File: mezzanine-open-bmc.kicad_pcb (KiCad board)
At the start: 2 copper layers, 85 x 54.1 mm, 53 parts, among them P1 CONN_02X20, P2 CONN_02X20, P3 CONN_01X04, P4 CONN_01X04, SW1 PWR, SW2 RST, U1 FT230XS, U2 SOT223, U3 DS3231N, U4 PCA9306, U5 M24C16-WMN6P, U6 REG_1.8V, U7 TXS0104PW

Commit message: Complete Schematic & Start PCB Layout
Pulling all the changes in.

Signed-off-by: Sophie Haynes <sophie.haynes@linaro.org>
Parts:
- added C16: 0.1n, Capacitors_SMD:C_0603, F.Cu at (151.4, 117.2)
- added C17: 0.1n, Capacitors_SMD:C_0603, F.Cu at (159.1, 114.8)
- added P5: CONN_01X04, 96boards:Grove_SMD_Connector, F.Cu at (205.2, 138.2)
- added R12: 2.2K, Resistors_SMD:R_0603, F.Cu at (156.2, 117.2)
- added R14: 2.2K, Resistors_SMD:R_0603, F.Cu at (149.8, 117.2)
- added R15: 2.2K, Resistors_SMD:R_0603, F.Cu at (158.0, 117.2)
- added R16: 200k, Resistors_SMD:R_0603, F.Cu at (150.5, 119.5)
- added R21: 200k, Resistors_SMD:R_0603, F.Cu at (159.6, 117.3)
- added R22: 0R, Resistors_SMD:R_1206, F.Cu at (162.0, 166.0)
- added R9: 2.2K, Resistors_SMD:R_0603, F.Cu at (148.1, 117.2)
- added U8: PCA9306, 96boards:PCA9306, F.Cu at (155.6, 111.9)
- C14, C15: value 100n -> 0.1n
- P3, P4: footprint 96boards:Grove4P -> 96boards:Grove_SMD_Connector
- R1, R13: value 90Ω -> 990R
- R10, R17: value 620R -> 22R
- U2: value SOT223 -> PMIC-CJT1117-3.3(SOT223)
- U7: value TXS0104PW -> PCA9306; footprint Housings_SSOP:SSOP-14_5.3x6.2mm_Pitch0.65mm -> 96boards:PCA9306
- moved U5 39.7 mm to (190.7, 122.0)
- moved C7 36.9 mm to (188.5, 115.8)
- moved C10 28.3 mm to (188.6, 107.3)
- moved C14 25.3 mm to (151.3, 109.7), turned to 90 degrees
- moved C15 25.1 mm to (155.6, 109.9), turned to 90 degrees
- moved U7 25.0 mm to (150.2, 112.0), turned to 0 degrees
- moved P4 24.0 mm to (206.8, 102.8), turned to 90 degrees
- moved P3 20.9 mm to (205.5, 120.8), turned to 90 degrees
- moved C9 15.7 mm to (153.2, 109.7)
- moved R6 15.4 mm to (107.5, 125.5)
- moved U4 14.2 mm to (152.9, 111.9), turned to 0 degrees
- moved C6 10.7 mm to (165.3, 123.2)
- moved U2 10.3 mm to (141.3, 118.5), turned to 90 degrees
- moved R18 9.86 mm to (152.9, 117.1), turned to 90 degrees
- moved C12 9.63 mm to (133.6, 126.5)
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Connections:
- C11 pad 1: Net-(C11-Pad1) -> +3V3_F
- C15 pad 1: +5V -> +1V8
- C6 pad 1: GND -> +5V
- C6 pad 2: +5V -> GND
- P3 pad 1: I2C0_SCL/5 -> I2C0_SCL_3.3
- P3 pad 2: I2C0_SDA/5 -> I2C0_SDA_3.3
- P3 pad 3: +5V -> +3V3
- P4 pad 1: I2C1_SCL/5 -> I2C1_SCL_3.3
- P4 pad 2: I2C1_SDA/5 -> I2C1_SDA_3.3
- P4 pad 3: +5V -> +3V3
- U1 pad 10: Net-(C11-Pad1) -> +3V3_F
- U1 pad 11: Net-(C11-Pad1) -> +3V3_F
- U5 pad 5: I2C0_SDA -> I2C0_SDA_3.3
- U5 pad 6: I2C0_SCL -> I2C0_SCL_3.3
- U7 pad 1: +1V8 -> GND
- U7 pad 2: I2C0_SDA -> +1V8
- U7 pad 3: I2C0_SCL -> I2C1_SCL_BMC
- U7 pad 4: I2C1_SDA -> I2C1_SDA_BMC
- U7 pad 5: I2C1_SCL -> I2C1_SDA_BMC_3.3
- U7 pad 6: Net-(U7-Pad6) -> I2C1_SCL_BMC_3.3
- U7 pad 7: GND -> Net-(C16-Pad1)
- U7 pad 8: +1V8 -> Net-(C16-Pad1)
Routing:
- net +1V8: track 187.7 -> 50.0 mm
- net +5V: track 166.3 -> 58.9 mm, vias 3 -> 2
- net GND: track 153.9 -> 75.6 mm
- net I2C0_SCL: track 72.4 -> 11.6 mm, vias 3 -> 2
- net I2C0_SDA: track 68.8 -> 10.6 mm
- net I2C1_SCL_BMC: track 0.00 -> 29.9 mm, vias 0 -> 1
- net PWR_BTN_BMC: track 19.0 -> 47.8 mm, vias 1 -> 2
- net I2C1_SDA_BMC: track 0.00 -> 27.9 mm, vias 0 -> 1
- net UART1_RX_BMC: track 26.2 -> 1.49 mm, vias 1 -> 0
- net Net-(BT1-Pad1): track 22.5 -> 0.00 mm, vias 1 -> 0
- net UART1_TX_BMC: track 20.6 -> 0.00 mm, vias 1 -> 0
- net I2C1_SCL: track 28.4 -> 10.5 mm, vias 2 -> 0
- net I2C1_SDA: track 27.3 -> 10.5 mm, vias 2 -> 0
- net I2C1_SCL/5: track 16.5 -> 0.00 mm
- net VBUS: track 15.9 -> 1.75 mm
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- added copper zone on B.Cu, net GND
- added copper zone on F.Cu, net GND
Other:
- board size 85 x 54.1 mm -> 85 x 54 mm

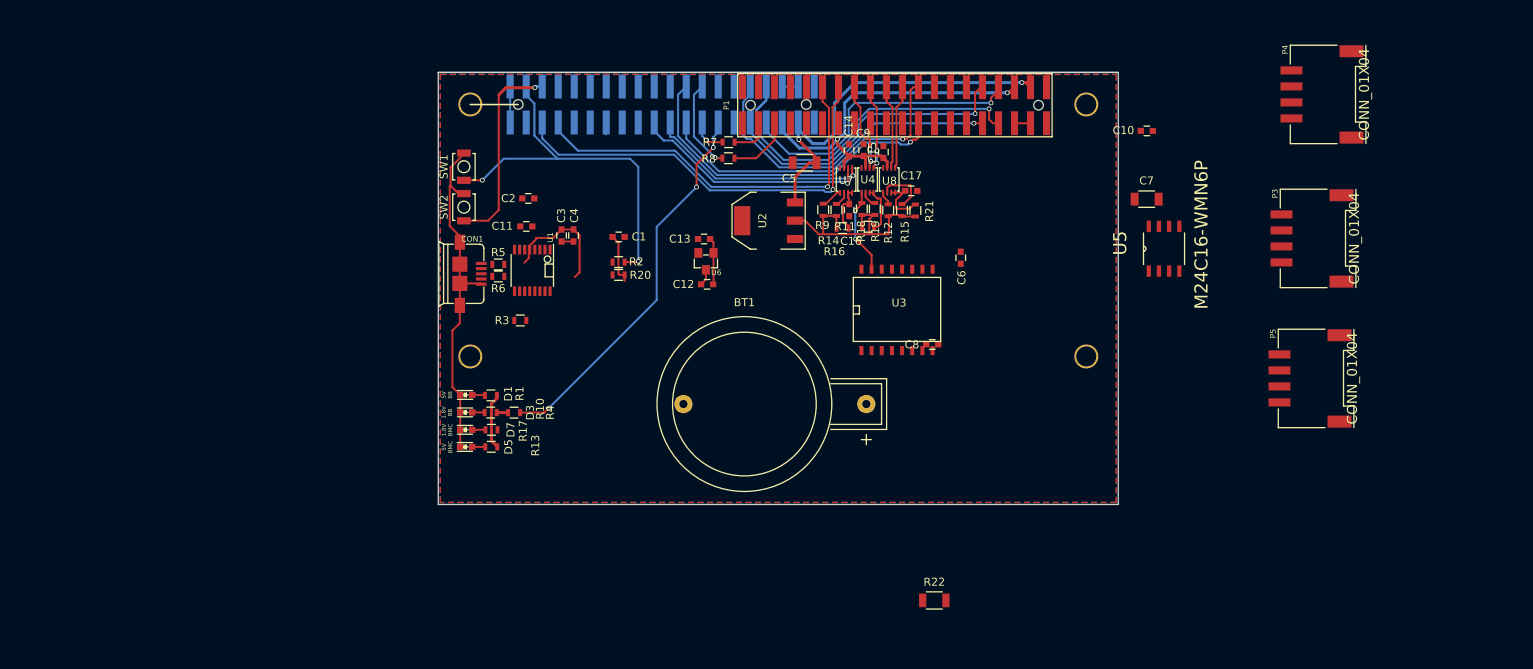
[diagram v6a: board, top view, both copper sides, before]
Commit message: Swap Location of P1/P2
The BMC board should be on the top, so the pin header have been switched
accordingly.

Signed-off-by: Sophie Haynes <sophie.haynes@linaro.org>
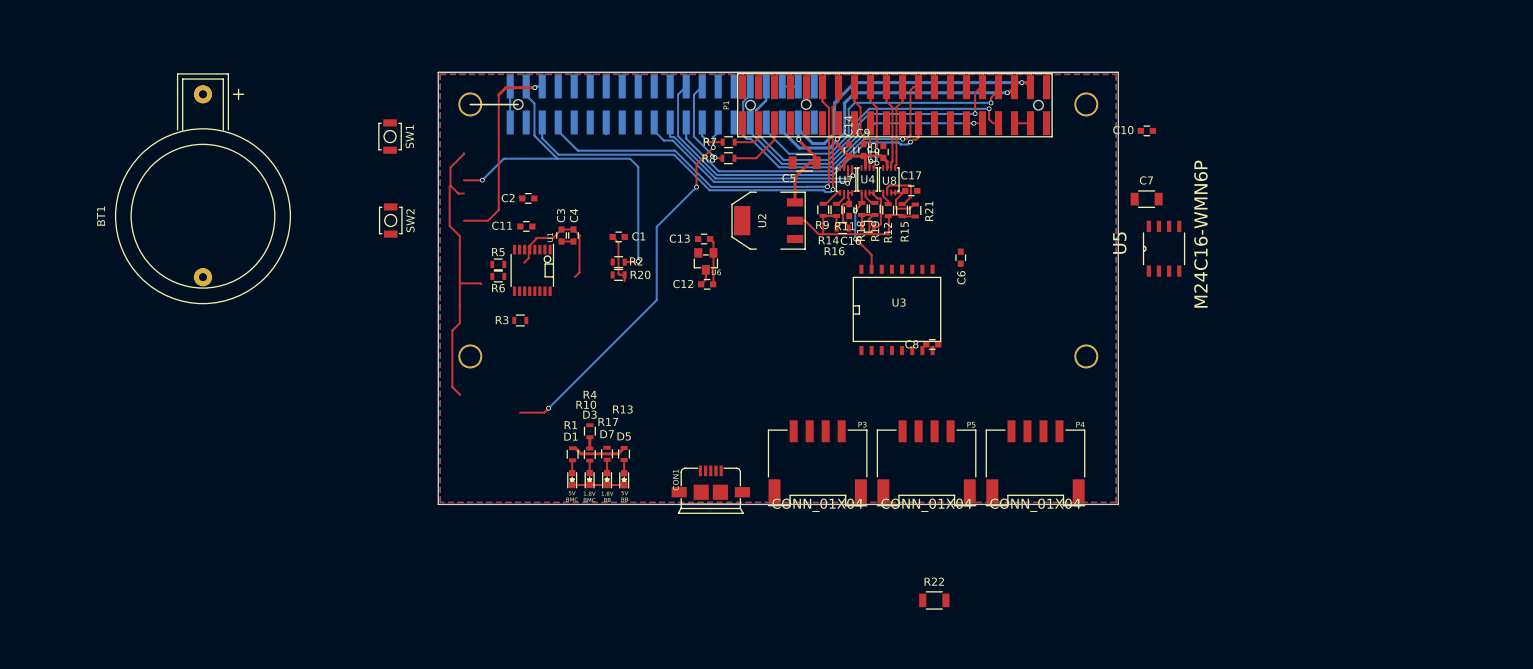
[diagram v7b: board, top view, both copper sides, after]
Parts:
- R11, R16, R21: value 200k -> 200K
- moved BT1 71.6 mm to (70.6, 118.0), turned to 90 degrees
- moved P3 62.9 mm to (147.4, 145.0), turned to 0 degrees
- moved P4 53.0 mm to (174.7, 145.0), turned to 0 degrees
- moved P5 44.7 mm to (161.0, 145.0), turned to 0 degrees
- moved CON1 43.7 mm to (134.1, 154.0), turned to 0 degrees
- moved D5 20.2 mm to (123.2, 150.8), turned to 90 degrees
- moved D7 18.7 mm to (121.1, 150.8), turned to 90 degrees
- moved D3 17.5 mm to (118.9, 150.8), turned to 90 degrees
- moved D1 16.9 mm to (116.7, 150.8), turned to 90 degrees
- moved R13 16.6 mm to (123.2, 147.7), turned to 270 degrees
- moved R17 14.8 mm to (121.1, 147.7), turned to 270 degrees
- moved R10 13.5 mm to (118.9, 147.8), turned to 270 degrees
- moved R1 12.6 mm to (116.8, 147.7), turned to 270 degrees
- moved SW1 9.97 mm to (94.0, 108.0), turned to 270 degrees
- moved R4 9.76 mm to (118.9, 144.8), turned to 90 degrees
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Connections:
- C1 pad 1: Net-(C1-Pad1) -> /USB+
- C2 pad 1: Net-(C2-Pad1) -> /USB-
- CON1 pad 2: Net-(C2-Pad1) -> /USB-
- CON1 pad 3: Net-(C1-Pad1) -> /USB+
- P1 pad 10: SPIO_DIN -> SPIO_DIN_BMC
- P1 pad 11: UART1_TX -> UART1_TX_BMC
- P1 pad 12: SPIO_CS -> SPIO_CS_BMC
- P1 pad 13: UART1_RX -> UART1_RX_BMC
- P1 pad 14: SPIO_DOUT -> SPIO_DOUT_BMC
- P1 pad 16: PCM_FS -> PCM_FS_BMC
- P1 pad 18: PCM_CLK -> PCM_CLK_BMC
- P1 pad 19: I2C1_SCL -> I2C1_SCL_BMC
- P1 pad 20: PCM_DO -> PCM_DO_BMC
- P1 pad 21: I2C1_SDA -> I2C1_SDA_BMC
- P1 pad 22: PCM_DI -> PCM_DI_BMC
- P1 pad 25: GPIO_C -> GPIO_C_BMC
- P1 pad 26: GPIO_D -> GPIO_D_BMC
- P1 pad 27: GPIO_E -> GPIO_E_BMC
- P1 pad 28: GPIO_F -> GPIO_F_BMC
- P1 pad 29: GPIO_G -> GPIO_G_BMC
- P1 pad 3: UART0_CTS -> Net-(P1-Pad3)
- P1 pad 30: GPIO_H -> GPIO_H_BMC
- P1 pad 36: SYS_DCIN -> SYS_DCIN_BMC
- P1 pad 38: SYS_DCIN -> SYS_DCIN_BMC
- P1 pad 4: PWR_BTN_N -> PWR_BTN_BMC
- P1 pad 5: UART0_TX -> UART1_RX
- P1 pad 6: RST_BTN_N -> RST_BTN_BMC
- P1 pad 7: UART0_RX -> UART1_TX
- P1 pad 8: SPIO_SCL -> SPIO_SCL_BMC
- P1 pad 9: UART0_RTS -> Net-(P1-Pad9)
- P2 pad 10: SPIO_DIN_BMC -> SPIO_DIN
- P2 pad 11: UART1_TX_BMC -> UART1_TX
- P2 pad 12: SPIO_CS_BMC -> SPIO_CS
- P2 pad 13: UART1_RX_BMC -> UART1_RX
- P2 pad 14: SPIO_DOUT_BMC -> SPIO_DOUT
- P2 pad 16: PCM_FS_BMC -> PCM_FS
- P2 pad 18: PCM_CLK_BMC -> PCM_CLK
- P2 pad 19: I2C1_SCL_BMC -> I2C1_SCL
- P2 pad 20: PCM_DO_BMC -> PCM_DO
- P2 pad 21: I2C1_SDA_BMC -> I2C1_SDA
- P2 pad 22: PCM_DI_BMC -> PCM_DI
- P2 pad 25: GPIO_C_BMC -> GPIO_C
- P2 pad 26: GPIO_D_BMC -> GPIO_D
- P2 pad 27: GPIO_E_BMC -> GPIO_E
- P2 pad 28: GPIO_F_BMC -> GPIO_F
- P2 pad 29: GPIO_G_BMC -> GPIO_G
- P2 pad 3: Net-(P2-Pad3) -> UART0_CTS
- P2 pad 30: GPIO_H_BMC -> GPIO_H
- P2 pad 36: SYS_DCIN_BMC -> SYS_DCIN
- P2 pad 38: SYS_DCIN_BMC -> SYS_DCIN
- P2 pad 4: PWR_BTN_BMC -> PWR_BTN_N
- P2 pad 5: UART1_RX -> UART0_TX
- P2 pad 6: RST_BTN_BMC -> RST_BTN_N
- P2 pad 7: UART1_TX -> UART0_RX
- P2 pad 8: SPIO_SCL_BMC -> SPIO_SCL
- P2 pad 9: Net-(P2-Pad9) -> UART0_RTS
- R14 pad 1: I2C1_SCL_BMC_3.3 -> +3V3
- R14 pad 2: +3V3 -> I2C1_SCL_BMC_3.3
- R15 pad 1: I2C1_SCL_3.3 -> +3V3
- R15 pad 2: +3V3 -> I2C1_SCL_3.3
- R19 pad 1: I2C0_SCL_3.3 -> +3V3
- R19 pad 2: +3V3 -> I2C0_SCL_3.3
- R5 pad 1: Net-(R5-Pad1) -> /USB-
- R5 pad 2: Net-(C2-Pad1) -> /USB-
- R6 pad 1: Net-(R6-Pad1) -> /USB+
- R6 pad 2: Net-(C1-Pad1) -> /USB+
- U1 pad 8: Net-(R6-Pad1) -> /USB+
- U1 pad 9: Net-(R5-Pad1) -> /USB-
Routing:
- net UART1_RX: track 55.4 -> 1.49 mm, vias 1 -> 0
- net UART1_TX: track 51.5 -> 0.00 mm, vias 1 -> 0
- net GPIO_E_BMC: track 48.3 -> 0.00 mm, vias 3 -> 0
- net GPIO_E: track 0.00 -> 48.3 mm, vias 0 -> 3
- net UART0_TX: track 0.00 -> 42.3 mm, vias 0 -> 1
- net UART0_RX: track 0.00 -> 37.6 mm, vias 0 -> 1
- net GND: track 75.6 -> 38.7 mm
- net (no net): track 0.00 -> 36.9 mm
- net I2C1_SDA_BMC: track 27.9 -> 3.23 mm
- net I2C1_SDA: track 10.5 -> 35.1 mm
- net RST_BTN_N: track 8.05 -> 31.1 mm, vias 0 -> 1
- net RST_BTN_BMC: track 25.2 -> 2.09 mm, vias 1 -> 0
- net UART1_TX_BMC: track 0.00 -> 13.9 mm
- net UART1_RX_BMC: track 1.49 -> 13.1 mm
- net GPIO_D_BMC: track 11.4 -> 0.97 mm
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
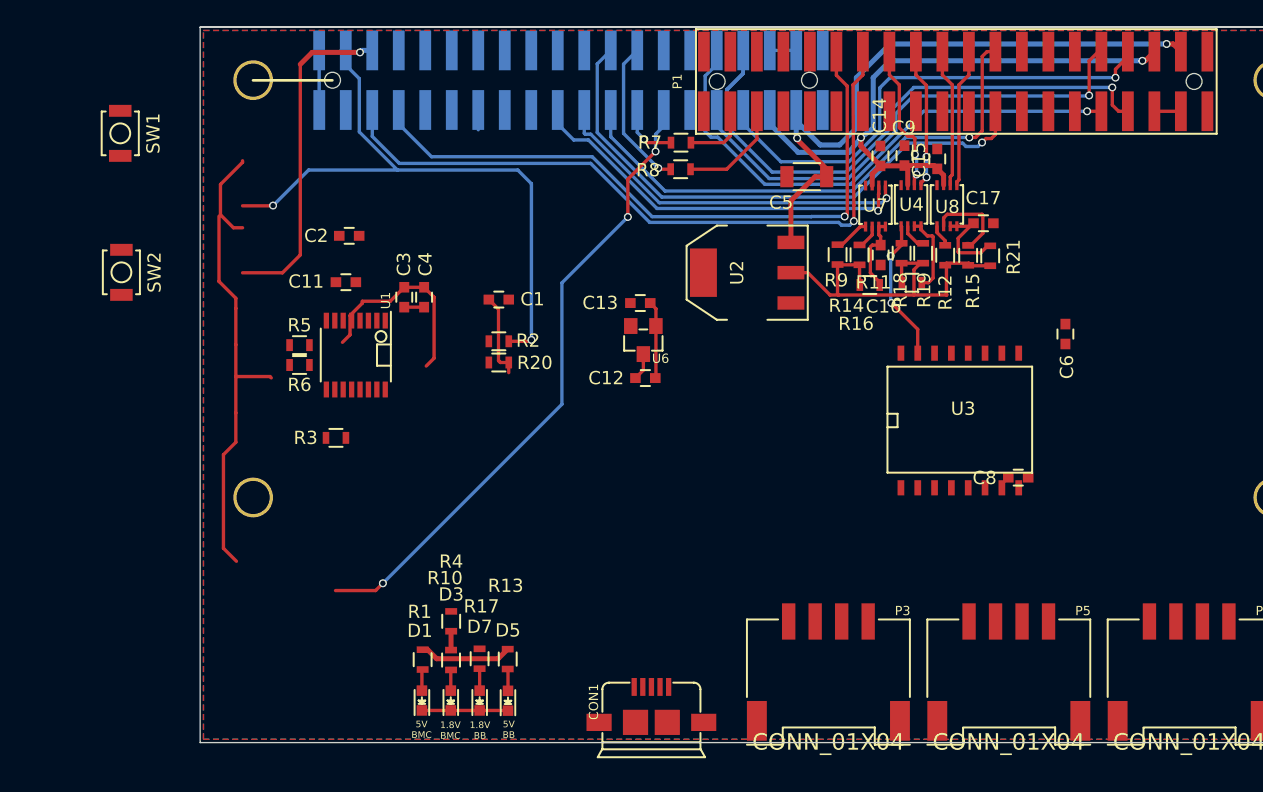
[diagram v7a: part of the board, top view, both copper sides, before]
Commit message: Change Push Switches to Slide Toggle
Since this is a stackable board, it could be awkward to access push buttons.
These have been changed to sliders for usability.

Signed-off-by: Sophie Haynes <sophie.haynes@linaro.org>
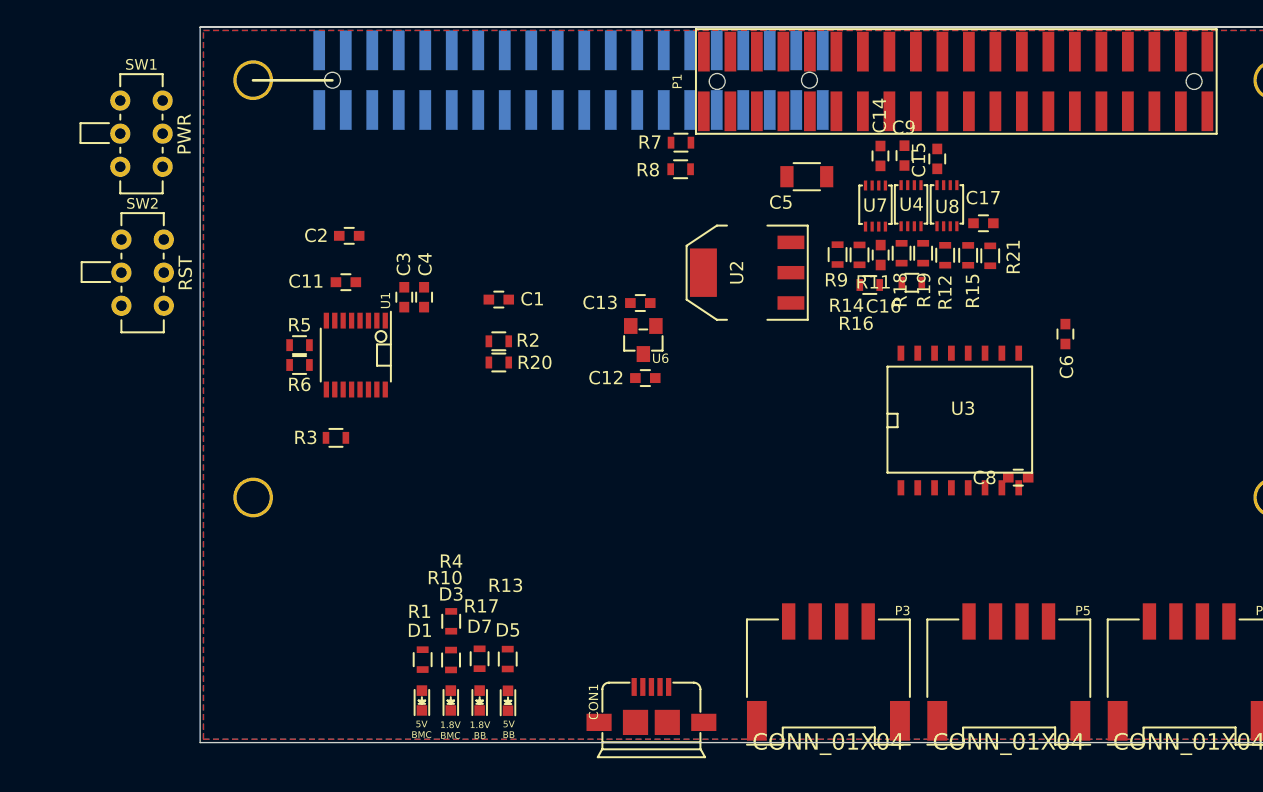
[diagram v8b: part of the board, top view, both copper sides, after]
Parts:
- SW1, SW2: footprint Buttons_Switches_SMD:SW_SPST_B3U-1000P -> 96boards:DIP_Toggle_Switch
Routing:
- net +5V: track 58.9 -> 0.00 mm, vias 2 -> 0
- net GPIO_L: track 50.5 -> 0.00 mm, vias 1 -> 0
- net +1V8: track 50.0 -> 0.00 mm, vias 2 -> 0
- net GPIO_E: track 48.3 -> 0.00 mm, vias 3 -> 0
- net PWR_BTN_BMC: track 42.8 -> 0.00 mm, vias 2 -> 0
- net GPIO_B: track 42.6 -> 0.00 mm, vias 1 -> 0
- net UART0_TX: track 42.3 -> 0.00 mm, vias 1 -> 0
- net GPIO_A: track 41.5 -> 0.00 mm, vias 1 -> 0
- net GPIO_J: track 40.3 -> 0.00 mm, vias 1 -> 0
- net GND: track 38.7 -> 0.00 mm
- net GPIO_I: track 38.2 -> 0.00 mm, vias 1 -> 0
- net UART0_RX: track 37.6 -> 0.00 mm, vias 1 -> 0
- net GPIO_K: track 37.2 -> 0.00 mm, vias 1 -> 0
- net (no net): track 36.9 -> 0.00 mm
- net +3V3: track 35.7 -> 0.00 mm
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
